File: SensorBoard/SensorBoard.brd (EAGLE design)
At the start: 160 x 100 mm, 24 parts, among them IC1 7805, J1 DCJ0202, U1 CY8C5XXX-100PIN, X2 22-23-2051, X3 MINI-USB-SCHIELD-32005-201

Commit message: added stuff to board
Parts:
- added ACCELEROMETER: MPU-6000QFN-24, SparkFun-Sensors:QFN-24-TESTING
- added GPS: COPERNICUSSMD, SparkFun-RF:COPERNICUS
- added WIFI: WIFLY_GSX, SparkFun-RF:WIFLY_GSX
- moved X2 11.5 mm to (41.9, 6.35), turned to 0 degrees
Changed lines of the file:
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@@
 <element name="C9" library="rcl" package="C0402" value="0.1uF" x="100.33" y="35.56"/>
 <element name="C10" library="rcl" package="C0402" value="1uF" x="105.41" y="36.83" rot="R270"/>
-<element name="X2" library="con-molex" package="22-23-2051" value="22-23-2051" x="30.48" y="5.08" rot="R180">
-<attribute name="OC_NEWARK" value="38C9178" x="10.16" y="48.26" size="1.778" layer="27" rot="R180" display="off"/>
-<attribute name="MPN" value="22-23-2051" x="10.16" y="48.26" size="1.778" layer="27" rot="R180" display="off"/>
-<attribute name="MF" value="MOLEX" x="10.16" y="48.26" size="1.778" layer="27" rot="R180" display="off"/>
-<attribute name="OC_FARNELL" value="1462952" x="10.16" y="48.26" size="1.778" layer="27" rot="R180" display="off"/>
+<element name="X2" library="con-molex" package="22-23-2051" value="22-23-2051" x="41.91" y="6.35">
+<attribute name="OC_NEWARK" value="38C9178" x="62.23" y="-36.83" size="1.778" layer="27" display="off"/>
+<attribute name="MPN" value="22-23-2051" x="62.23" y="-36.83" size="1.778" layer="27" display="off"/>
+<attribute name="MF" value="MOLEX" x="62.23" y="-36.83" size="1.778" layer="27" display="off"/>
+<attribute name="OC_FARNELL" value="1462952" x="62.23" y="-36.83" size="1.778" layer="27" display="off"/>
 </element>
 <element name="3.3VREG" library="MYPARTS" package="LT1763IS8-SMD" value="LT1763IS8-3.3" x="24.13" y="29.21" rot="R90"/>
@@
 <attribute name="OC_FARNELL" value="1824860" x="-44.45" y="-39.37" size="1.778" layer="27" rot="R270" display="off"/>
 </element>
+<element name="GPS" library="SparkFun-RF" package="COPERNICUS" value="COPERNICUSSMD" x="114.3" y="96.52"/>
+<element name="WIFI" library="SparkFun-RF" package="WIFLY_GSX" value="WIFLY_GSX" x="138.43" y="60.96"/>
+<element name="ACCELEROMETER" library="SparkFun-Sensors" package="QFN-24-TESTING" value="MPU-6000QFN-24" x="151.13" y="7.62"/>
 </elements>
 <signals>
@@
 <wire x1="16.23" y1="10.16" x2="13.32" y2="20.32" width="0" layer="19" extent="1-1"/>
 <wire x1="11.43" y1="7.16" x2="16.23" y2="10.16" width="0" layer="19" extent="1-1"/>
-<wire x1="33.02" y1="5.08" x2="16.23" y2="10.16" width="0" layer="19" extent="1-1"/>
+<wire x1="39.37" y1="6.35" x2="16.23" y2="10.16" width="0" layer="19" extent="1-1"/>
 </signal>
 <signal name="+12V">
@@
 <wire x1="13.97" y1="26.67" x2="39.216" y2="87.895" width="0" layer="19" extent="1-1"/>
 <wire x1="14.62" y1="20.32" x2="13.97" y2="26.67" width="0" layer="19" extent="1-1"/>
-<wire x1="35.56" y1="5.08" x2="14.62" y2="20.32" width="0" layer="19" extent="1-1"/>
+<wire x1="36.83" y1="6.35" x2="14.62" y2="20.32" width="0" layer="19" extent="1-1"/>
 </signal>
 <signal name="N$1">
@@
 <contactref element="X2" pad="5"/>
 <contactref element="U1" pad="20"/>
-<wire x1="25.4" y1="5.08" x2="93.55" y2="47.3" width="0" layer="19" extent="1-1"/>
+<wire x1="46.99" y1="6.35" x2="93.55" y2="47.3" width="0" layer="19" extent="1-1"/>
 </signal>
 <signal name="SCLK">
 <contactref element="X2" pad="4"/>
 <contactref element="U1" pad="21"/>
-<wire x1="27.94" y1="5.08" x2="93.55" y2="46.8" width="0" layer="19" extent="1-1"/>
+<wire x1="44.45" y1="6.35" x2="93.55" y2="46.8" width="0" layer="19" extent="1-1"/>
 </signal>
 <signal name="XRES">
 <contactref element="X2" pad="3"/>
 <contactref element="U1" pad="15"/>
-<wire x1="30.48" y1="5.08" x2="93.55" y2="49.8" width="0" layer="19" extent="1-1"/>
+<wire x1="41.91" y1="6.35" x2="93.55" y2="49.8" width="0" layer="19" extent="1-1"/>
 </signal>
 <signal name="+3.3V">

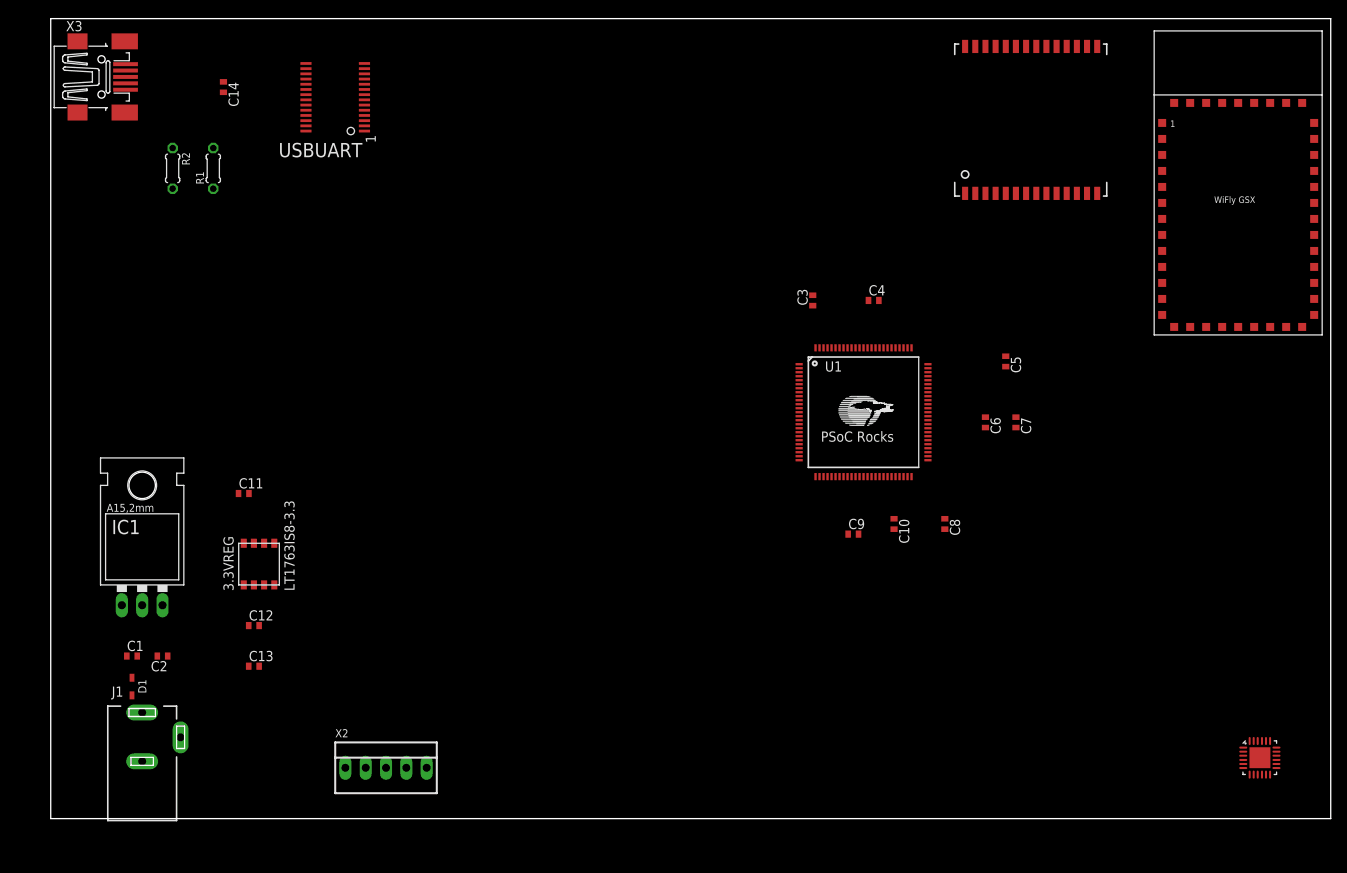
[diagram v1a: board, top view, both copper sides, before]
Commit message: wired up wifi - jack
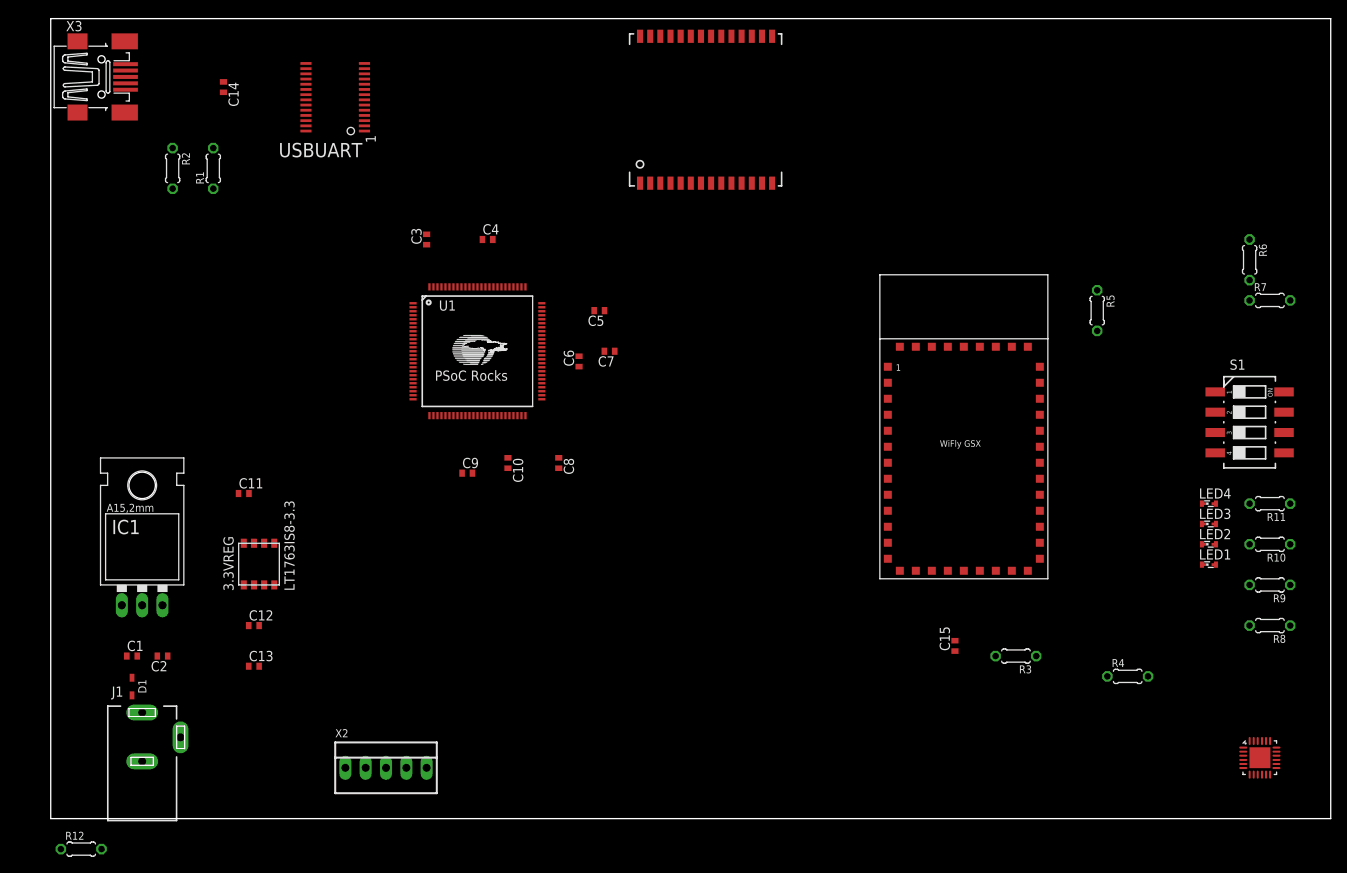
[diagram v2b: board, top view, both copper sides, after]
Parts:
- added C15: 47uF, rcl:C0402
- added LED1, LED2, LED3, LED4: (no value), led:SMARTLED-TTW
- added R10, R11, R7, R8, R9: 10k, resistor:0204/5
- added R12: 49k, resistor:0204/5
- added R3, R4, R5: SHUNT, resistor:0204/5
- added R6: 22k, resistor:0204/5
- added S1: 219-04, switch-dil:CTS-219-04
- moved C7 51.6 mm to (69.8, 58.4), turned to 180 degrees
- moved C6 51.4 mm to (66.0, 57.1), turned to 90 degrees
- moved C5 51.2 mm to (68.6, 63.5), turned to 180 degrees
- moved C4 48.9 mm to (54.6, 72.4)
- moved C8 48.9 mm to (63.5, 44.5)
- moved C10 48.9 mm to (57.1, 44.5)
- moved C3 48.9 mm to (47.0, 72.4)
- moved C9 48.9 mm to (52.1, 43.2)
- moved U1 48.9 mm to (53.3, 58.4)
- moved WIFI 45.9 mm to (104.1, 30.5)
- moved GPS 40.7 mm to (73.7, 97.8)
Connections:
- new net CTSIN: WIFI.11
- new net DRX: WIFI.23
- new net DTX: WIFI.22
- new net N$11: S1.8
- new net N$18: R3.1, WIFI.21
- new net N$19: R4.2, R5.2, WIFI.35
- new net N$20: R5.1, WIFI.18
- new net N$23: R6.2, R7.1, WIFI.34
- new net N$4: LED1.C@1, R8.2
- new net N$7: LED2.C@1, R9.2
- new net N$8: LED3.C@1, R10.2
- new net N$9: LED4.C@1, R11.2
- new net PIO4: LED4.A@1, WIFI.29
- new net PIO5: LED3.A@1, WIFI.28
- new net PIO6: LED2.A@1, WIFI.27
- new net PIO7: LED1.A@1, WIFI.26
- new net PIO8: WIFI.25
- new net PIO9: S1.1, WIFI.24
- new net RESET: WIFI.5
- new net RTSOUT: WIFI.10
- new net RXDIN: R6.1, WIFI.12
- new net SENS1: S1.2, WIFI.30
- new net SENS2: S1.3, WIFI.31
- new net SENS3: S1.4, WIFI.32
- new net TXSOUT: WIFI.13
- new net WAKE: WIFI.9
- net +3.3V: now also C15.1, R12.1, R3.2, WIFI.20
- net GND: now also C15.2, R10.1, R11.1, R4.1, R7.2, R8.1, R9.1, S1.5, S1.6, S1.7, WIFI.19, WIFI.36, WIFI.37, WIFI.38, WIFI.39, WIFI.40, WIFI.41, WIFI.42, WIFI.43, WIFI.44

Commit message: added stuff to board
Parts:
- removed ACCELEROMETER: MPU-6000QFN-24, SparkFun-Sensors:QFN-24-TESTING
- removed C15: 47uF, rcl:C0402
- removed GPS: COPERNICUSSMD, SparkFun-RF:COPERNICUS
- removed LED1, LED2, LED3, LED4: (no value), led:SMARTLED-TTW
- removed R10, R11, R7, R8, R9: 10k, resistor:0204/5
- removed R12: 49k, resistor:0204/5
- removed R3, R4, R5: SHUNT, resistor:0204/5
- removed R6: 22k, resistor:0204/5
- removed S1: 219-04, switch-dil:CTS-219-04
- removed WIFI: WIFLY_GSX, SparkFun-RF:WIFLY_GSX
- added GPS1, GPS2, GPS3, GPS4: COPERNICUSSMD, SparkFun-RF:COPERNICUS
- added U$1, U$2, U$3, U$4: ANTENNA2SMD, SparkFun-RF:ANTENNA-CHIP2
- added X1, X4, X5, X6: 22-23-2041, con-molex:22-23-2041
- renumbered U1 to CY8C5868AXI-LP035
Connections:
- removed net CTSIN: WIFI.11
- removed net DRX: WIFI.23
- removed net DTX: WIFI.22
- removed net N$11: S1.8
- removed net N$18: R3.1, WIFI.21
- removed net N$19: R4.2, R5.2, WIFI.35
- removed net N$20: R5.1, WIFI.18
- removed net N$23: R6.2, R7.1, WIFI.34
- removed net N$4: LED1.C@1, R8.2
- removed net N$7: LED2.C@1, R9.2
- removed net N$8: LED3.C@1, R10.2
- removed net N$9: LED4.C@1, R11.2
- removed net PIO4: LED4.A@1, WIFI.29
- removed net PIO5: LED3.A@1, WIFI.28
- removed net PIO6: LED2.A@1, WIFI.27
- removed net PIO7: LED1.A@1, WIFI.26
- removed net PIO8: WIFI.25
- removed net PIO9: S1.1, WIFI.24
- removed net RESET: WIFI.5
- removed net RTSOUT: WIFI.10
- removed net RXDIN: R6.1, WIFI.12
- removed net SENS1: S1.2, WIFI.30
- removed net SENS2: S1.3, WIFI.31
- removed net SENS3: S1.4, WIFI.32
- removed net TXSOUT: WIFI.13
- removed net WAKE: WIFI.9
- new net GPS1RXA: GPS1.21
- new net GPS1RXB: GPS1.20
- new net GPS1TXA: GPS1.23
- new net GPS1TXB: GPS1.22
- new net GPS1XSTB: GPS1.16
- new net GPS2RXA: GPS2.21
- new net GPS2RXB: GPS2.20
- new net GPS2TXA: GPS2.23
- new net GPS2TXB: GPS2.22
- new net GPS2XSTB: GPS2.16
- new net GPS3RXA: GPS3.21
- new net GPS3RXB: GPS3.20
- new net GPS3TXA: GPS3.23
- new net GPS3TXB: GPS3.22
- new net GPS3XSTB: GPS3.16
- new net GPS4RXA: GPS4.21
- new net GPS4RXB: GPS4.20
- new net GPS4TXA: GPS4.23
- new net GPS4TXB: GPS4.22
- new net GPS4XSTB: GPS4.16
- new net N$10: GPS1.3, U$1.FEED
- new net N$12: GPS2.3, U$2.FEED
- new net N$13: GPS3.3, U$3.FEED
- new net N$14: GPS4.3, U$4.FEED
- new net RX1: X1.4
- new net RX2: X4.4
- new net RX3: X5.4
- new net RX4: X6.4
- new net TX1: X1.3
- new net TX2: X4.3
- new net TX3: X5.3
- new net TX4: X6.3
- net +3.3V: now also GPS1.12, GPS2.12, GPS3.12, GPS4.12; no longer C15.1, R12.1, R3.2, WIFI.20
- net +5V: now also X1.2, X4.2, X5.2, X6.2
- net GND: now also GPS1.1, GPS1.13, GPS1.14, GPS1.15, GPS1.2, GPS1.27, GPS1.28, GPS1.4, GPS1.7, GPS2.1, GPS2.13, GPS2.14, GPS2.15, GPS2.2, GPS2.27, GPS2.28, GPS2.4, GPS2.7, GPS3.1, GPS3.13, GPS3.14, GPS3.15, GPS3.2, GPS3.27, GPS3.28, GPS3.4, GPS3.7, GPS4.1, GPS4.13, GPS4.14, GPS4.15, GPS4.2, GPS4.27, GPS4.28, GPS4.4, GPS4.7, X1.1, X4.1, X5.1, X6.1; no longer C15.2, R10.1, R11.1, R4.1, R7.2, R8.1, R9.1, S1.5, S1.6, S1.7, WIFI.19, WIFI.36, WIFI.37, WIFI.38, WIFI.39, WIFI.40, WIFI.41, WIFI.42, WIFI.43, WIFI.44

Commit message: wired up gps
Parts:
- removed X1, X4, X5, X6: 22-23-2041, con-molex:22-23-2041
- added PWR: GREEN, led:SMARTLED-TTW
- added R3: 4k, resistor:0204/5
- added X10, X8, X9: (no value), con-molex:KK-156-4
- added X7: (no value), con-molex:KK-156-5
- X2: value 22-23-2051 -> (none); device con-molex:22-23-2051 -> con-molex:KK-156-4
- moved X2 122.2 mm to (148.6, 66.0), turned to 180 degrees
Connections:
- new net N$4: PWR.A@1, R3.1
- net +5V: now also R3.2, X10.2, X2.2, X7.1, X8.2, X9.2; no longer X1.2, X2.1, X4.2, X5.2, X6.2
- net GND: now also PWR.C@1, X10.1, X2.1, X7.2, X8.1, X9.1; no longer X1.1, X2.2, X4.1, X5.1, X6.1
- net GPS1RXA: now also CY8C5868AXI-LP035.7
- net GPS1RXB: now also CY8C5868AXI-LP035.9
- net GPS1TXA: now also CY8C5868AXI-LP035.6
- net GPS1TXB: now also CY8C5868AXI-LP035.8
- net GPS1XSTB: now also CY8C5868AXI-LP035.22
- net GPS2RXA: now also CY8C5868AXI-LP035.98
- net GPS2RXB: now also CY8C5868AXI-LP035.96
- net GPS2TXA: now also CY8C5868AXI-LP035.99
- net GPS2TXB: now also CY8C5868AXI-LP035.97
- net GPS2XSTB: now also CY8C5868AXI-LP035.23
- net GPS3RXA: now also CY8C5868AXI-LP035.94
- net GPS3RXB: now also CY8C5868AXI-LP035.92
- net GPS3TXA: now also CY8C5868AXI-LP035.95
- net GPS3TXB: now also CY8C5868AXI-LP035.93
- net GPS3XSTB: now also CY8C5868AXI-LP035.24
- net GPS4RXA: now also CY8C5868AXI-LP035.78
- net GPS4RXB: now also CY8C5868AXI-LP035.76
- net GPS4TXA: now also CY8C5868AXI-LP035.79
- net GPS4TXB: now also CY8C5868AXI-LP035.77
- net GPS4XSTB: now also CY8C5868AXI-LP035.25
- net RX1: now also X2.4; no longer X1.4
- net RX2: now also X8.4; no longer X4.4
- net RX3: now also X9.4; no longer X5.4
- net RX4: now also X10.4; no longer X6.4
- net SCLK: now also X7.4; no longer X2.4
- net SDAT: now also X7.5; no longer X2.5
- net TX1: now also X2.3; no longer X1.3
- net TX2: now also X8.3; no longer X4.3
- net TX3: now also X9.3; no longer X5.3
- net TX4: now also X10.3; no longer X6.3
- net XRES: now also X7.3; no longer X2.3

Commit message: fixed pin
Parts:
- added C15, C17: .1uF, rcl:C0402
- added C16: 10nF, rcl:C0402
- added C18: 2.2nF, rcl:C0402
- added U$5: HMC5883LSMD, SparkFun-Sensors:16LPCC
- added U1: MPU-6000QFN-24, SparkFun-Sensors:QFN-24-TESTING
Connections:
- new net AUXCL1: U1.7
- new net AUXDA1: U1.6
- new net CLKOUT1: U1.22
- new net FSYNC: U1.11
- new net INT1: U1.12
- new net N$7: C15.1, U1.10
- new net N$8: U1.20
- new net SCL: U1.23
- new net SDA: U1.24
- net +3.3V: now also C16.1, C17.1, U1.13, U1.8
- net GND: now also C15.2, C16.2, C17.2, C18.2, U1.1, U1.18, U1.9
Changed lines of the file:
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@@
 <element name="PWR" library="led" package="SMARTLED-TTW" value="GREEN" x="53.34" y="26.67"/>
 <element name="R3" library="resistor" package="0204/5" value="4k" x="53.34" y="19.05" rot="R270"/>
+<element name="U1" library="SparkFun-Sensors" package="QFN-24-TESTING" value="MPU-6000QFN-24" x="22.86" y="67.31"/>
+<element name="C15" library="rcl" package="C0402" value=".1uF" x="11.43" y="68.58"/>
+<element name="C16" library="rcl" package="C0402" value="10nF" x="11.43" y="57.15"/>
+<element name="C17" library="rcl" package="C0402" value=".1uF" x="25.4" y="57.15"/>
+<element name="C18" library="rcl" package="C0402" value="2.2nF" x="31.75" y="68.58"/>
+<element name="U$5" library="SparkFun-Sensors" package="16LPCC" value="HMC5883LSMD" x="-2.54" y="2.54"/>
 </elements>
 <signals>
@@
 <contactref element="X2" pad="1"/>
 <contactref element="PWR" pad="C@1"/>
+<contactref element="U1" pad="9"/>
+<contactref element="U1" pad="18"/>
+<contactref element="U1" pad="1"/>
+<contactref element="C15" pad="2"/>
+<contactref element="C16" pad="2"/>
+<contactref element="C17" pad="2"/>
+<contactref element="C18" pad="2"/>
 <wire x1="128.27" y1="92.71" x2="128.27" y2="93.98" width="0" layer="19" extent="1-1"/>
 <wire x1="128.27" y1="77.47" x2="128.27" y2="92.71" width="0" layer="19" extent="1-1"/>
@@
 <wire x1="57.15" y1="43.8" x2="52.72" y2="43.18" width="0" layer="19" extent="1-1"/>
 <wire x1="63.5" y1="43.8" x2="57.15" y2="43.8" width="0" layer="19" extent="1-1"/>
+<wire x1="53.34" y1="27.17" x2="52.72" y2="43.18" width="0" layer="19" extent="1-1"/>
 <wire x1="78.1558" y1="77.47" x2="67.93" y2="63.5" width="0" layer="19" extent="1-1"/>
 <wire x1="78.1558" y1="78.74" x2="78.1558" y2="77.47" width="0" layer="19" extent="1-1"/>
@@
 <wire x1="15.24" y1="83.82" x2="21.59" y2="90.79" width="0" layer="19" extent="1-1"/>
 <wire x1="9.35" y1="94.31" x2="15.24" y2="83.82" width="0" layer="19" extent="1-1"/>
-<wire x1="24.78" y1="40.64" x2="45.29" y2="57.92" width="0" layer="19" extent="1-1"/>
-<wire x1="25.4" y1="34.417" x2="24.78" y2="40.64" width="0" layer="19" extent="1-1"/>
-<wire x1="26.67" y1="34.417" x2="25.4" y2="34.417" width="0" layer="19" extent="1-1"/>
-<wire x1="26.67" y1="29.21" x2="26.67" y2="34.417" width="0" layer="19" extent="1-1"/>
+<wire x1="26.67" y1="29.21" x2="53.34" y2="27.17" width="0" layer="19" extent="1-1"/>
 <wire x1="26.05" y1="24.13" x2="26.67" y2="29.21" width="0" layer="19" extent="1-1"/>
+<wire x1="26.67" y1="34.417" x2="26.67" y2="29.21" width="0" layer="19" extent="1-1"/>
+<wire x1="25.4" y1="34.417" x2="26.67" y2="34.417" width="0" layer="19" extent="1-1"/>
+<wire x1="24.78" y1="40.64" x2="25.4" y2="34.417" width="0" layer="19" extent="1-1"/>
 <wire x1="13.32" y1="20.32" x2="26.05" y2="24.13" width="0" layer="19" extent="1-1"/>
 <wire x1="10.81" y1="20.32" x2="13.32" y2="20.32" width="0" layer="19" extent="1-1"/>
@@
 <wire x1="11.43" y1="7.16" x2="16.23" y2="10.16" width="0" layer="19" extent="1-1"/>
 <wire x1="25.25" y1="6.35" x2="16.23" y2="10.16" width="0" layer="19" extent="1-1"/>
-<wire x1="53.34" y1="27.17" x2="11.43" y2="7.16" width="0" layer="19" extent="1-1"/>
+<wire x1="24.9462" y1="68.5667" x2="11.43" y2="7.16" width="0" layer="19" extent="1-1"/>
+<wire x1="22.6025" y1="65.1884" x2="24.9462" y2="68.5667" width="0" layer="19" extent="1-1"/>
+<wire x1="20.7938" y1="68.5667" x2="22.6025" y2="65.1884" width="0" layer="19" extent="1-1"/>
+<wire x1="12.08" y1="68.58" x2="22.6025" y2="65.1884" width="0" layer="19" extent="1-1"/>
+<wire x1="12.08" y1="57.15" x2="12.08" y2="68.58" width="0" layer="19" extent="1-1"/>
+<wire x1="26.05" y1="57.15" x2="12.08" y2="57.15" width="0" layer="19" extent="1-1"/>
+<wire x1="32.4" y1="68.58" x2="26.05" y2="57.15" width="0" layer="19" extent="1-1"/>
 <wire x1="154.53" y1="66.04" x2="128.27" y2="77.47" width="0" layer="19" extent="1-1"/>
 <wire x1="154.53" y1="53.34" x2="154.53" y2="66.04" width="0" layer="19" extent="1-1"/>
@@
 <wire x1="39.216" y1="87.895" x2="46.99" y2="71.74" width="0" layer="19" extent="1-1"/>
 <wire x1="31.904" y1="91.145" x2="39.216" y2="87.895" width="0" layer="19" extent="1-1"/>
-<wire x1="13.97" y1="26.67" x2="47.34" y2="50.37" width="0" layer="19" extent="1-1"/>
-<wire x1="14.62" y1="20.32" x2="13.97" y2="26.67" width="0" layer="19" extent="1-1"/>
-<wire x1="21.29" y1="6.35" x2="14.62" y2="20.32" width="0" layer="19" extent="1-1"/>
-<wire x1="53.34" y1="16.51" x2="21.29" y2="6.35" width="0" layer="19" extent="1-1"/>
+<wire x1="53.34" y1="16.51" x2="51.42" y2="43.18" width="0" layer="19" extent="1-1"/>
+<wire x1="21.29" y1="6.35" x2="53.34" y2="16.51" width="0" layer="19" extent="1-1"/>
+<wire x1="14.62" y1="20.32" x2="21.29" y2="6.35" width="0" layer="19" extent="1-1"/>
+<wire x1="13.97" y1="26.67" x2="14.62" y2="20.32" width="0" layer="19" extent="1-1"/>
 </signal>
 <signal name="N$1">
@@
 <contactref element="GPS3" pad="12"/>
 <contactref element="GPS4" pad="12"/>
+<contactref element="U1" pad="13"/>
+<contactref element="C16" pad="1"/>
+<contactref element="U1" pad="8"/>
+<contactref element="C17" pad="1"/>
 <wire x1="78.1558" y1="80.01" x2="109.9058" y2="80.01" width="0" layer="19" extent="1-1"/>
 <wire x1="97.79" y1="42.5958" x2="109.9058" y2="80.01" width="0" layer="19" extent="1-1"/>
 <wire x1="101.6" y1="5.7658" x2="97.79" y2="42.5958" width="0" layer="19" extent="1-1"/>
-<wire x1="25.4" y1="29.21" x2="78.1558" y2="80.01" width="0" layer="19" extent="1-1"/>
+<wire x1="24.9462" y1="66.0133" x2="78.1558" y2="80.01" width="0" layer="19" extent="1-1"/>
+<wire x1="22.0979" y1="65.1884" x2="24.9462" y2="66.0133" width="0" layer="19" extent="1-1"/>
+<wire x1="24.75" y1="57.15" x2="22.0979" y2="65.1884" width="0" layer="19" extent="1-1"/>
+<wire x1="10.78" y1="57.15" x2="22.0979" y2="65.1884" width="0" layer="19" extent="1-1"/>
+<wire x1="25.4" y1="29.21" x2="24.75" y2="57.15" width="0" layer="19" extent="1-1"/>
 <wire x1="24.13" y1="29.21" x2="25.4" y2="29.21" width="0" layer="19" extent="1-1"/>
 <wire x1="24.75" y1="24.13" x2="24.13" y2="29.21" width="0" layer="19" extent="1-1"/>
@@
 <wire x1="53.34" y1="26.17" x2="53.34" y2="21.59" width="0" layer="19" extent="1-1"/>
 </signal>
+<signal name="SDA">
+<contactref element="U1" pad="24"/>
+</signal>
+<signal name="N$7">
+<contactref element="U1" pad="10"/>
+<contactref element="C15" pad="1"/>
+<wire x1="23.1375" y1="65.1884" x2="10.78" y2="68.58" width="0" layer="19" extent="1-1"/>
+</signal>
+<signal name="N$8">
+<contactref element="U1" pad="20"/>
+</signal>
+<signal name="INT1">
+<contactref element="U1" pad="12"/>
+</signal>
+<signal name="FSYNC">
+<contactref element="U1" pad="11"/>
+</signal>
+<signal name="AUXCL1">
+<contactref element="U1" pad="7"/>
+</signal>
+<signal name="AUXDA1">
+<contactref element="U1" pad="6"/>
+</signal>
+<signal name="CLKOUT1">
+<contactref element="U1" pad="22"/>
+</signal>
+<signal name="SCL">
+<contactref element="U1" pad="23"/>
+</signal>
 </signals>
